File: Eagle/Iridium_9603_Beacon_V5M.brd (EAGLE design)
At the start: 67.6 x 132 mm, 103 parts, among them CON4 uFL, J1 SS4-10-3.50-X-D, Q1 DMG3415U-7, Q2 DMG3415U-7, Q3 DMG3415U-7, Q4 DMG3415U-7, Q5 2N2222, U1 MCP111T-240E/TT, U2 SPX3819-3.3, U3 LTC3225EDDB#TRMPBF, U4 MPL3115A2LGA8, U5 ATSAMD21G18_QFN, U6 MAX-M8, U7 LT1634-1,25BMCMS8, X1 32.768

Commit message: preliminary changes to V5M board
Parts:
- added U$40, U$48, U$49, U$50, U$51, U$52: (no value), holes:3,2
- moved CON1 55.8 mm to (58.2, 14.0)
- moved CS 30.2 mm to (89.8, 102.1)
- moved GND2 30.2 mm to (89.8, 104.6)
- moved MISO 30.2 mm to (84.7, 104.6)
- moved SCK 30.2 mm to (84.7, 102.1)
- moved 3V3 30.2 mm to (87.3, 104.6)
- moved MOSI 30.2 mm to (87.3, 102.1)
- moved RST 30.1 mm to (87.2, 85.0)
- moved SWDIO 30.1 mm to (87.2, 87.5)
- moved BAT- 30.1 mm to (89.7, 85.0)
- moved GND 30.1 mm to (89.7, 87.5)
- moved SWCLK 30.1 mm to (84.6, 87.5)
- moved VBUS 30.1 mm to (84.6, 85.0)
- moved R15 20.4 mm to (58.2, 107.7)
- moved R17 20.4 mm to (58.2, 91.7)
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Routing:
- net GND: track 692.6 -> 887.5 mm
- net D+: track 28.6 -> 83.1 mm
- net D-: track 29.9 -> 84.5 mm
- net N$16: track 2.85 -> 57.3 mm
- net SD_CS: track 23.3 -> 33.2 mm
- net MOSI: track 25.5 -> 35.3 mm
- net MISO: track 23.1 -> 33.0 mm
- net SCK: track 22.6 -> 32.5 mm
- net +3V3: track 195.2 -> 205.1 mm
- net !RESET: track 57.4 -> 67.2 mm
- net VBUS: track 156.3 -> 166.1 mm
- net SWCLK: track 22.0 -> 31.6 mm
- net SWDIO: track 24.2 -> 33.8 mm
- net N$15: track 18.2 -> 24.6 mm
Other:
- board size 67.6 x 132 mm -> 76 x 120.7 mm
- board text added: "Iridium 9603N Beacon V5M"

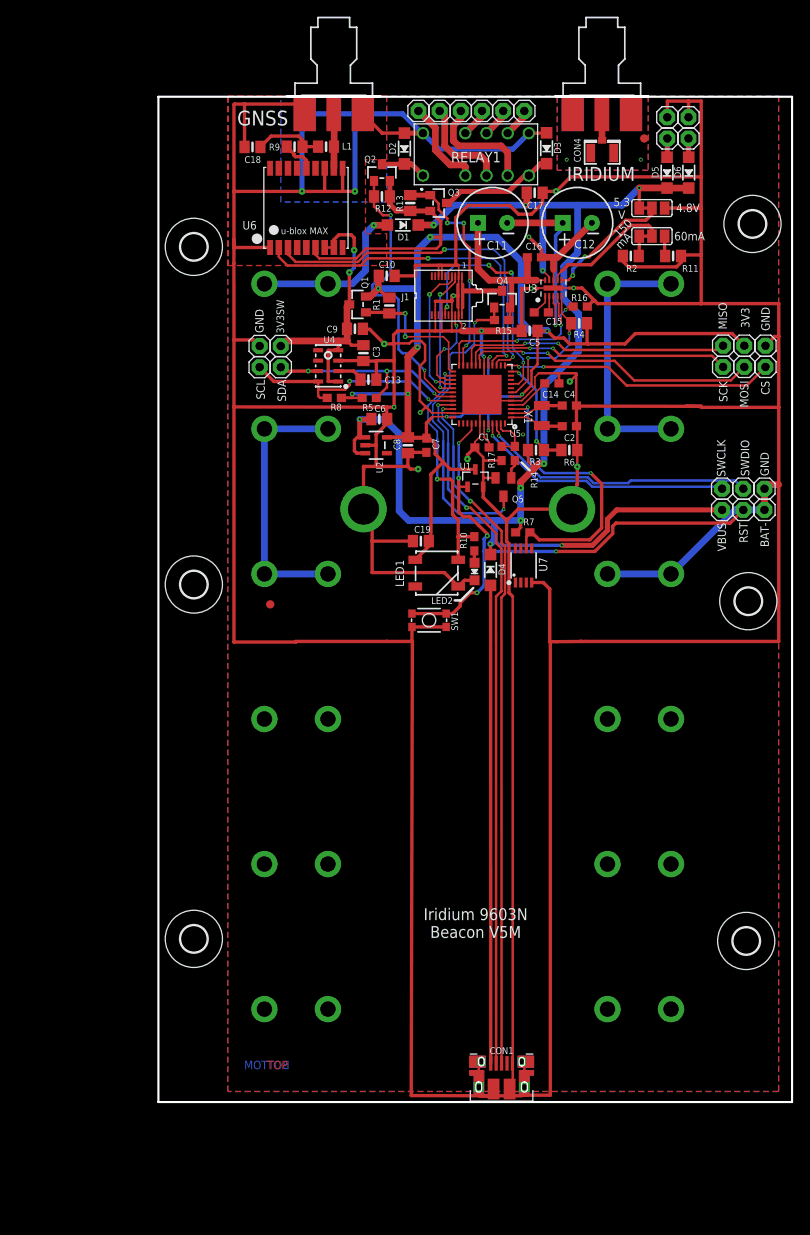
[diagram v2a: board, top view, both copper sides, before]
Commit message: removing backup eagle files, edits to V5M PCB board
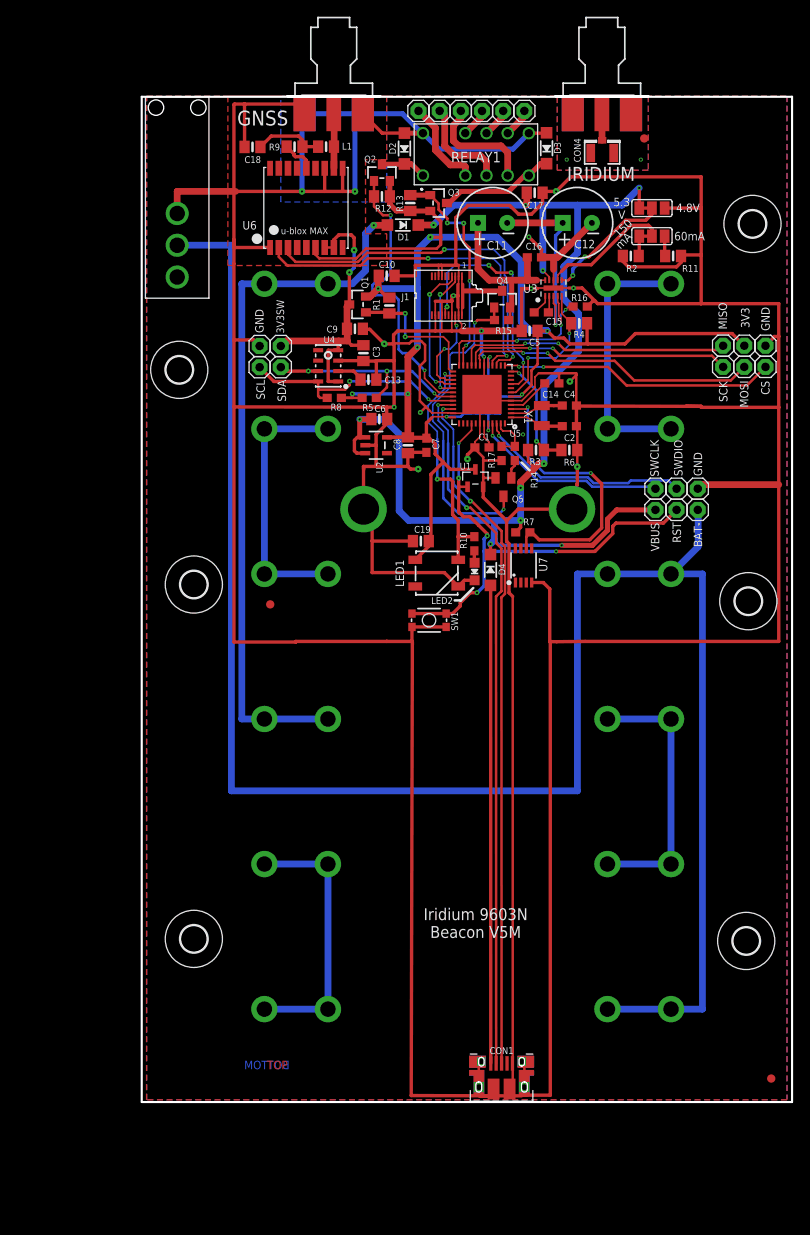
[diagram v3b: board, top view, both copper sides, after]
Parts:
- removed D5, D6: MBR120, microbuilder:SOD-123
- removed SOLAR1+, SOLAR1-, SOLAR2+, SOLAR2-: (no value), adafruit:1X01
- added FD3: FIDUCIAL1X2, SparkFun-Aesthetics:FIDUCIAL-1X2
- added U$53: 7101K2AV2QE, argol-eagle-library:AV2_SPDT
- moved U$52 14.9 mm to (19.5, 101.8)
- moved BAT- 8.00 mm to (81.7, 85.0)
- moved GND 8.00 mm to (81.7, 87.5)
- moved RST 8.00 mm to (79.2, 85.0)
- moved SWCLK 8.00 mm to (76.6, 87.5)
- moved SWDIO 8.00 mm to (79.2, 87.5)
- moved VBUS 8.00 mm to (76.6, 85.0)
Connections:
- removed net N$14: D5.A, SOLAR2+.1
- removed net N$4: D6.A, SOLAR1+.1
- net GND: now also U$53.P$1; no longer SOLAR1-.1, SOLAR2-.1
- net N$15: now also U$53.P$2
- net VBUS: no longer D5.C, D6.C
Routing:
- net N$15: track 24.6 -> 227.0 mm
- net VBAT: track 20.3 -> 85.7 mm
- net N$22: track 0.00 -> 33.3 mm
- net N$29: track 0.00 -> 32.6 mm
- net VBUS: track 166.1 -> 152.2 mm
- net SWDIO: track 33.8 -> 25.8 mm
- net SWCLK: track 31.6 -> 23.6 mm
- net !RESET: track 67.2 -> 59.2 mm
- net N$4: track 2.28 -> 0.00 mm
- net N$14: track 2.28 -> 0.00 mm
- net GND: track 887.5 -> 888.1 mm
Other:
- board size 76 x 120.7 mm -> 78 x 120.7 mm

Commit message: Clean version of board modifications.  Extra batteries, switch added.  Reset button flipped to bottom.  Moved USB port.  NO EXTRA serial port yet.
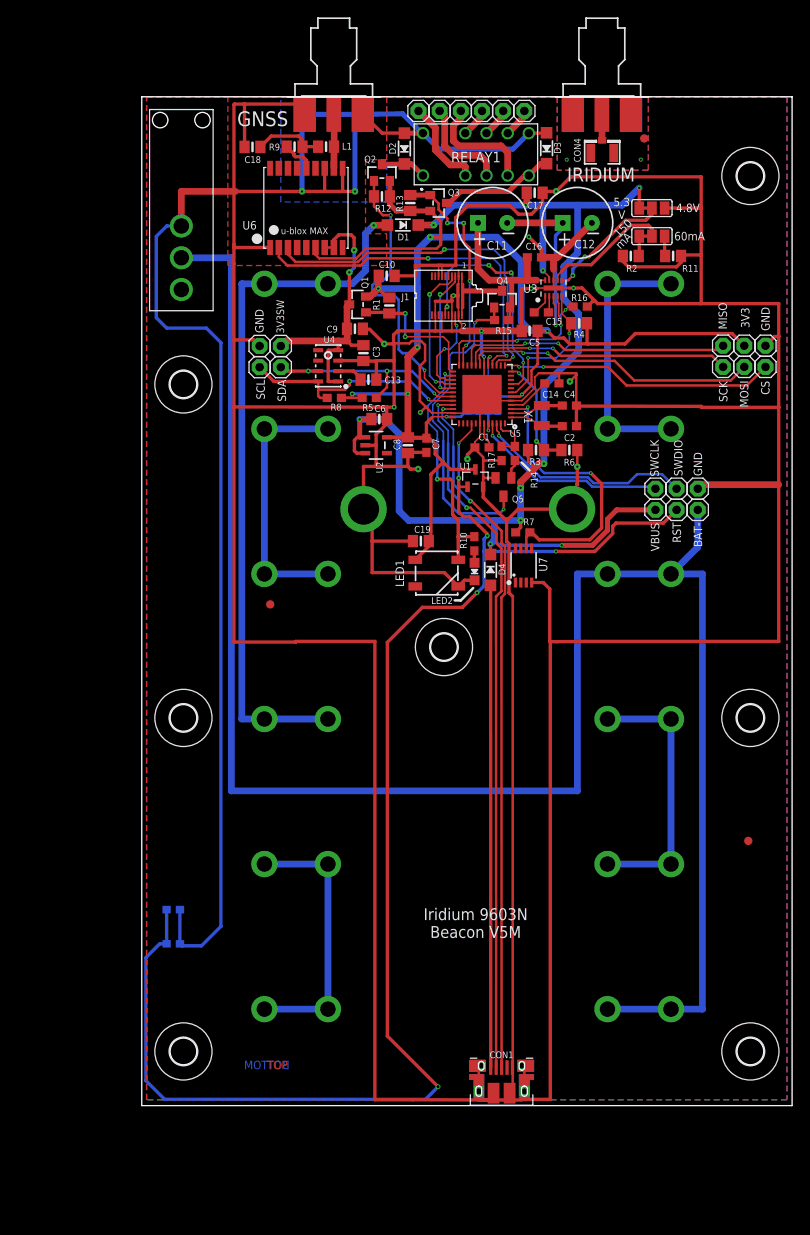
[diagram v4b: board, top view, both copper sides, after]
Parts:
- added U$2: (no value), holes:3,2
- moved SW1 47.9 mm to (18.8, 35.0), flipped to the bottom, turned to 90 degrees
- moved FD3 28.6 mm to (87.8, 45.2)
- moved U$50 16.0 mm to (20.0, 60.0)
- moved U$49 14.0 mm to (88.0, 60.0)
- moved U$48 13.6 mm to (20.0, 20.0)
- moved U$40 13.3 mm to (88.0, 20.0)
- moved U$51 5.76 mm to (88.0, 125.0)
- moved U$52 1.82 mm to (20.0, 100.0)
- moved U$53 1.58 mm to (19.8, 119.0)
- moved CON1 0.50 mm to (58.2, 13.5)
- moved GNSS 0.08 mm to (38.0, 134.5)
- moved IRIDIUM 0.08 mm to (70.2, 134.5)
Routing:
- net !RESET: track 59.2 -> 177.8 mm, vias 5 -> 6
- net GND: track 888.1 -> 978.1 mm, vias 17 -> 16
- net N$15: track 227.0 -> 225.1 mm
- net +3V3: track 205.1 -> 203.8 mm
- net N$22: track 33.3 -> 32.6 mm
- net SWDIO: track 25.8 -> 26.4 mm
- net D+: track 83.1 -> 83.6 mm
- net D-: track 84.5 -> 85.0 mm
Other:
- board size 78 x 120.7 mm -> 78 x 121 mm

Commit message: several changes to the board layout. Switched digital I/O lines for coil reset and charger shutdown.  Added extra serial port.
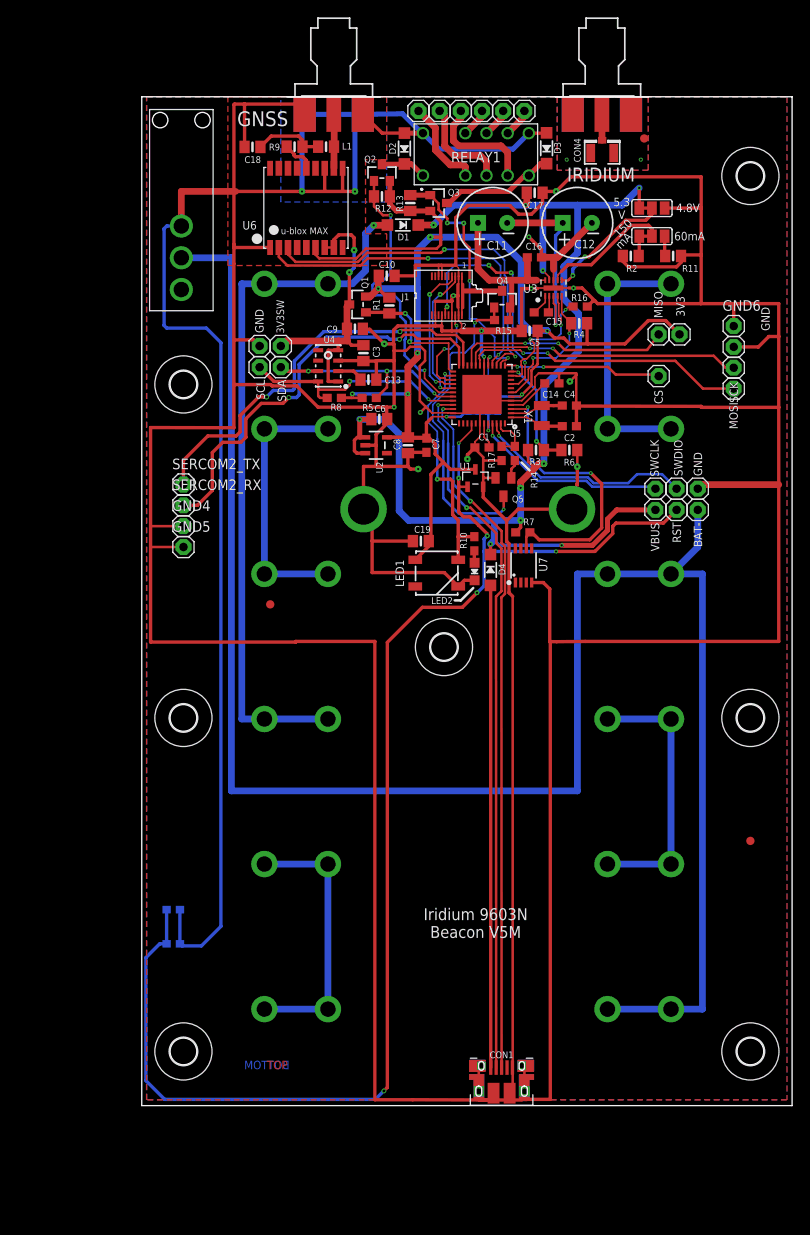
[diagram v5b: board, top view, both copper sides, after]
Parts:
- added GND4, GND5, GND6, SERCOM2_RX, SERCOM2_TX: (no value), adafruit:1X01
- moved CS 12.9 mm to (77.0, 101.0)
- moved 3V3 7.89 mm to (79.5, 106.0)
- moved MISO 7.85 mm to (77.0, 106.0)
- moved GND2 3.81 mm to (86.0, 104.5)
- moved MOSI 2.89 mm to (86.0, 99.5)
- moved SCK 1.27 mm to (86.0, 102.0)
- moved FD3 0.25 mm to (88.0, 45.2)
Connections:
- net D2: now also SERCOM2_TX.1; no longer Q3.1, R13.1
- net D3: now also Q3.1, R13.1
- net D5: now also SERCOM2_RX.1; no longer R16.1, U3.4
- net D8: now also R16.1, U3.4
- net GND: now also GND4.1, GND5.1, GND6.1
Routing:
- net GND: track 978.1 -> 1012.8 mm
- net D3: track 0.00 -> 29.7 mm, vias 0 -> 4
- net D5: track 23.2 -> 50.6 mm, vias 3 -> 2
- net D2: track 26.2 -> 49.4 mm, vias 4 -> 2
- net D8: track 0.00 -> 18.6 mm, vias 0 -> 3
- net SD_CS: track 33.2 -> 19.1 mm
- net !RESET: track 177.8 -> 169.2 mm
- net +3V3: track 203.8 -> 196.8 mm
- net MISO: track 33.0 -> 26.0 mm
- net MOSI: track 35.3 -> 33.9 mm
- net SCK: track 32.4 -> 33.8 mm
- net D0: track 42.5 -> 41.5 mm
- net D6: track 15.8 -> 16.6 mm
- net D1: track 42.9 -> 43.6 mm

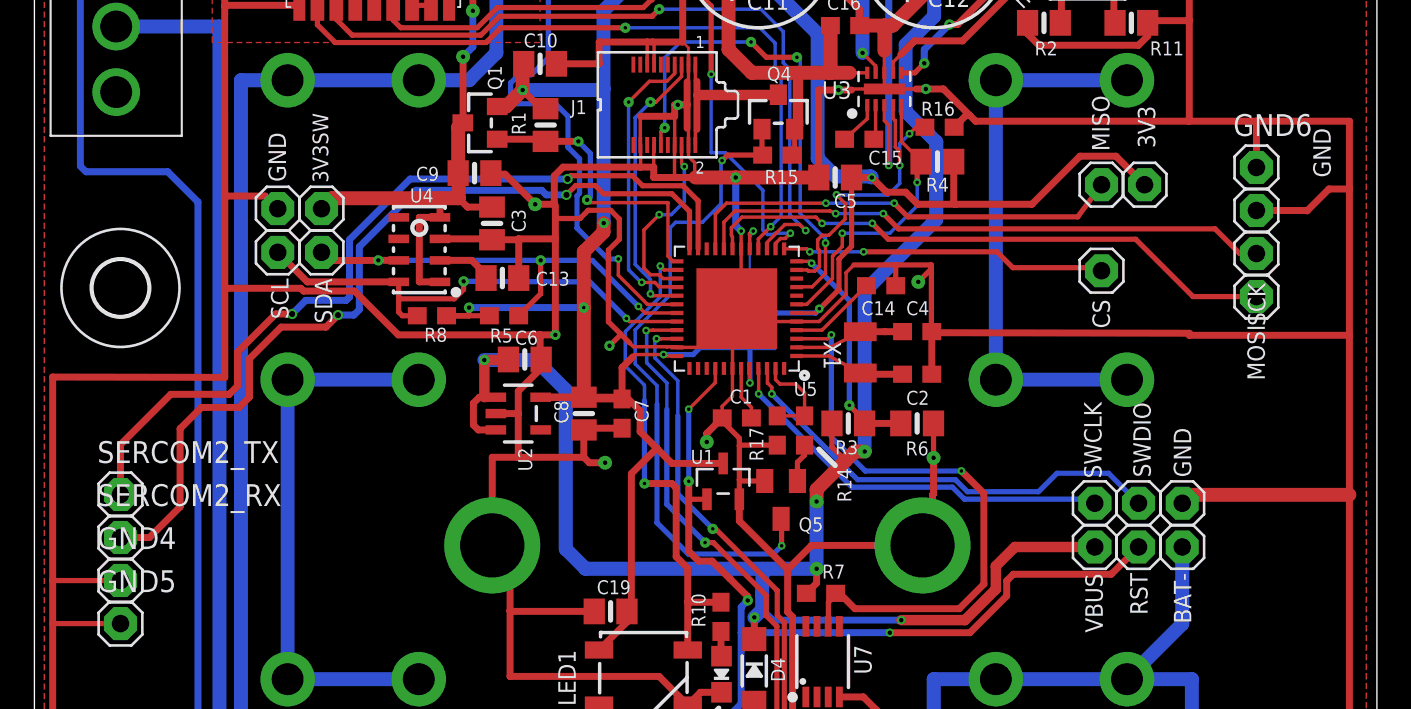
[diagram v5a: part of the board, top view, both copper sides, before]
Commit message: updated CAD file, BOM, Gerber files generated for initial version of the board
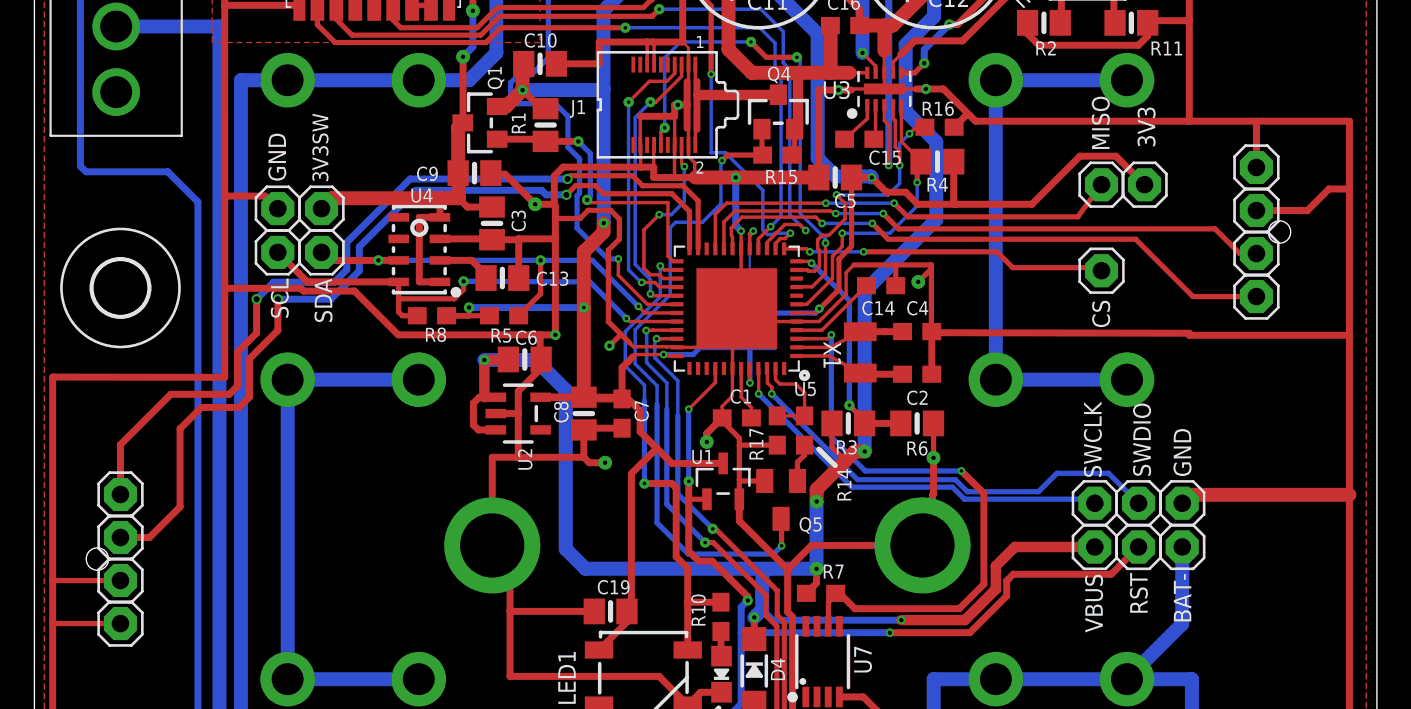
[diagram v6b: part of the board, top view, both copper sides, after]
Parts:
- C2, C4: value 22pF -> 12pF
- R10: value 2.2K -> 1K
- renumbered U$53 to U53
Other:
- board text removed: "Iridium 9603N Beacon V5"
